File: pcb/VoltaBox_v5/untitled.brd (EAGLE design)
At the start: 100 x 80 mm, 46 parts, among them J1 1050170001, Q1 8 MHz, Q2 32768Hz, U1 MCU-STM32F103RCT6(LQFP64), U2 ADUM1401WTRWZ, U4 LMP92064SD/NOPB, X1 112J-TDAR-R(MICROSD)

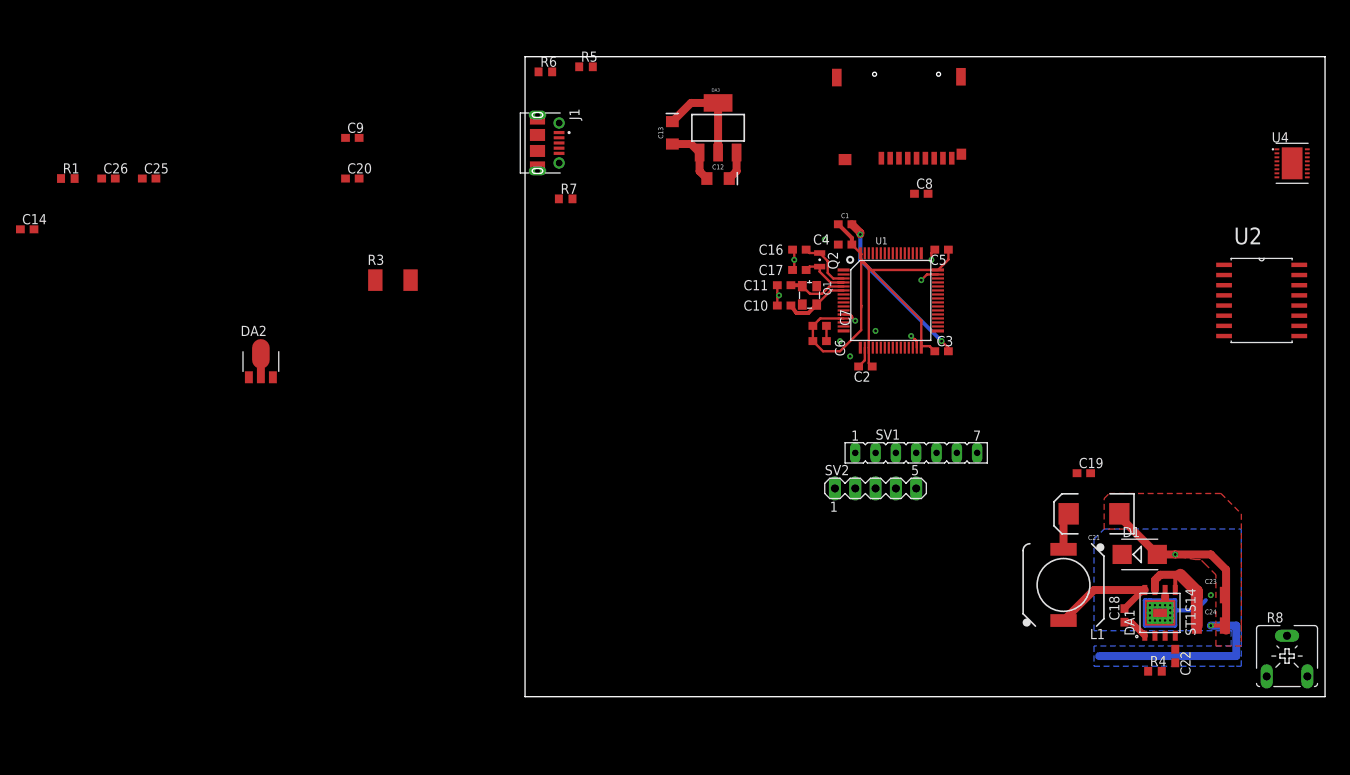
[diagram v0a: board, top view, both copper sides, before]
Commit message: Some PCB changes. ICs prefix changes. Added some capacitors. Q3 case type changed.
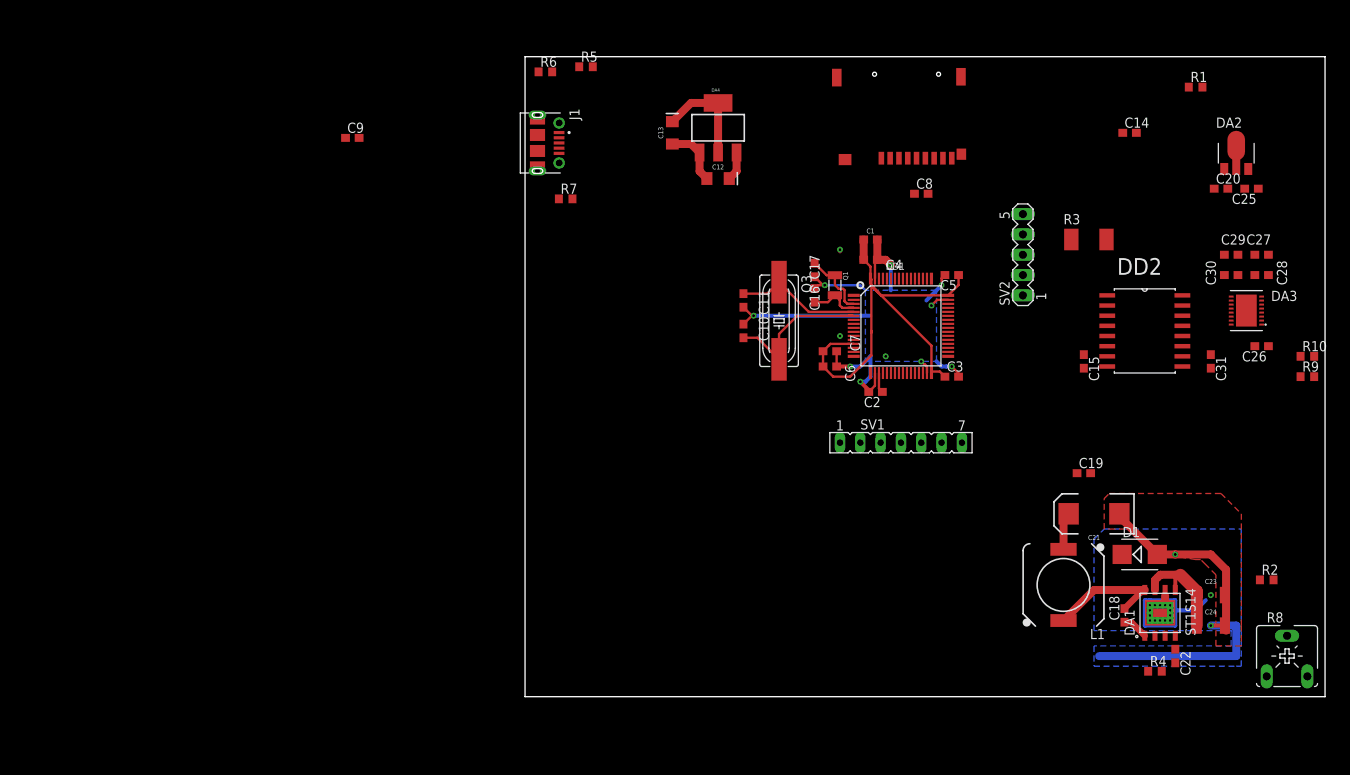
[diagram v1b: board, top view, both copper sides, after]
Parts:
- removed Q2: 32768Hz, crystal:FC-12M
- removed U1: MCU-STM32F103RCT6(LQFP64), MCU-STM32F103RCT6_LQFP64_:LQFP64-0.5-10X10MM
- removed U2: ADUM1401WTRWZ, ADUM1401WTRWZ:SOIC127P1032X265-16N
- removed U4: LMP92064SD/NOPB, LMP92064SD_NOPB:SON50P400X500X80-17N
- added C15, C28, C29, C31: 0.1u, eagle-ltspice:C0603
- added C27, C30: 10p, eagle-ltspice:C0603
- added DA4: (no value), SparkFun-IC-Power:SOT223
- added DD1: MCU-STM32F103RCT6(LQFP64), MCU-STM32F103RCT6_LQFP64_:LQFP64-0.5-10X10MM
- added DD2: ADUM1401WTRWZ, ADUM1401WTRWZ:SOIC127P1032X265-16N
- added Q3: 8MHz, crystal:HC49UP
- added R10, R2, R9: 3.3K, resistor:R0603
- DA3: value (none) -> LMP92064SD/NOPB; device SparkFun-IC-Power:SOT223 -> LMP92064SD_NOPB:SON50P400X500X80-17N
- Q1: value 8 MHz -> 32768Hz; device crystal-geyer_V1_0:3.2X2.5_KX-7 -> crystal-geyer_V1_0:3.2X1.5
- moved C26 145.7 mm to (92.1, 43.8), turned to 180 degrees
- moved R1 141.4 mm to (83.8, 76.2)
- moved C14 138.3 mm to (75.6, 70.5)
- moved C25 137.8 mm to (90.8, 63.5), turned to 180 degrees
- moved DA2 124.7 mm to (88.9, 67.9)
- moved C20 108.6 mm to (87.0, 63.5)
- moved R3 87.1 mm to (70.5, 57.1)
- moved DA3 69.9 mm to (90.2, 48.3), turned to 180 degrees
- moved SV2 34.5 mm to (62.2, 55.2), turned to 90 degrees
- moved C11 5.99 mm to (27.3, 45.7), turned to 90 degrees
- moved C10 5.43 mm to (27.3, 49.5), turned to 270 degrees
- moved C17 3.70 mm to (36.2, 50.2), turned to 90 degrees
- moved C1 3.70 mm to (43.2, 57.1)
- moved C4 3.70 mm to (43.2, 54.6), turned to 0 degrees
- moved C5 3.42 mm to (53.3, 52.7)
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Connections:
- new net N$24: R2.2, R8.A
- new net N$25: DA3.5, R10.1, R9.2
- net +3V3: now also C15.1, DA4.2, DA4.4, DD1.13, DD1.19, DD1.32, DD1.48, DD1.64, DD2.1, DD2.7; no longer DA3.2, DA3.4, U1.13, U1.19, U1.32, U1.48, U1.64, U2.1, U2.7
- net +4V: now also R10.2
- net +5V: now also C27.1, C28.1, C29.1, C30.1, C31.1, DA3.8, DA3.9, DD2.10, DD2.16; no longer U2.10, U2.16, U4.8, U4.9
- net ADC_MISO: now also DA3.11, DD1.35, DD2.6; no longer U1.35, U2.6, U4.11
- net ADC_MOSI: now also DD1.36, DD2.3; no longer U1.36, U2.3
- net ADC_NSS: now also DD1.33, DD2.5; no longer U1.33, U2.5
- net ADC_SCK: now also DD1.34, DD2.4; no longer U1.34, U2.4
- net GND: now also C15.2, C27.2, C28.2, C29.2, C30.2, C31.2, DA3.10, DA3.16, DA3.17, DA3.2, DA3.4, DA3.6, DA3.7, DA4.1, DD1.12, DD1.18, DD1.31, DD1.47, DD1.60, DD1.63, DD2.15, DD2.2, DD2.8, DD2.9, R2.1, R9.1; no longer DA3.1, R8.A, U1.12, U1.18, U1.31, U1.47, U1.60, U1.63, U2.15, U2.2, U2.8, U2.9, U4.10, U4.16, U4.2, U4.4, U4.6, U4.7
- net N$1: now also DD1.5, Q3.1; no longer Q1.1, U1.5
- net N$11: now also DA3.12, DD2.14; no longer U2.14, U4.12
- net N$13: now also DD1.54; no longer U1.54
- net N$14: now also DD1.53; no longer U1.53
- net N$15: now also DD1.52; no longer U1.52
- net N$16: now also DD1.51; no longer U1.51
- net N$18: now also DD1.40; no longer U1.40
- net N$19: now also DD1.39; no longer U1.39
- net N$2: now also DD1.6, Q3.2; no longer Q1.3, U1.6
- net N$20: now also DD1.45; no longer U1.45
- net N$21: now also DD1.44; no longer U1.44
- net N$23: now also DA3.3; no longer U4.3
- net N$3: now also DA3.1; no longer U4.1
- net N$5: now also DA3.13, DD2.13; no longer U2.13, U4.13
- net N$6: now also DA3.14, DD2.12; no longer U2.12, U4.14
- net N$7: now also DD1.4, Q1.2; no longer Q2.2, U1.4
- net N$8: now also DD1.3, Q1.1; no longer Q2.1, U1.3
- net NRESET: now also DD1.7; no longer U1.7
- net OLED_CS: now also DD1.50; no longer U1.50
- net OLED_DC: now also DD1.58; no longer U1.58
- net OLED_MOSI: now also DD1.57; no longer U1.57
- net OLED_RS: now also DD1.56; no longer U1.56
- net OLED_SCK: now also DD1.55; no longer U1.55
- net SWCLK: now also DD1.49; no longer U1.49
- net SWDIO: now also DD1.46; no longer U1.46
- net VCC: now also DA4.3; no longer DA3.3
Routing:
- net GND: track 116.6 -> 142.0 mm
- net N$2: track 8.22 -> 20.6 mm
- net +3V3: track 84.8 -> 75.4 mm
- net N$1: track 7.58 -> 15.9 mm
- net N$8: track 7.04 -> 8.52 mm

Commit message: DC-DC new layout, adc part implemented
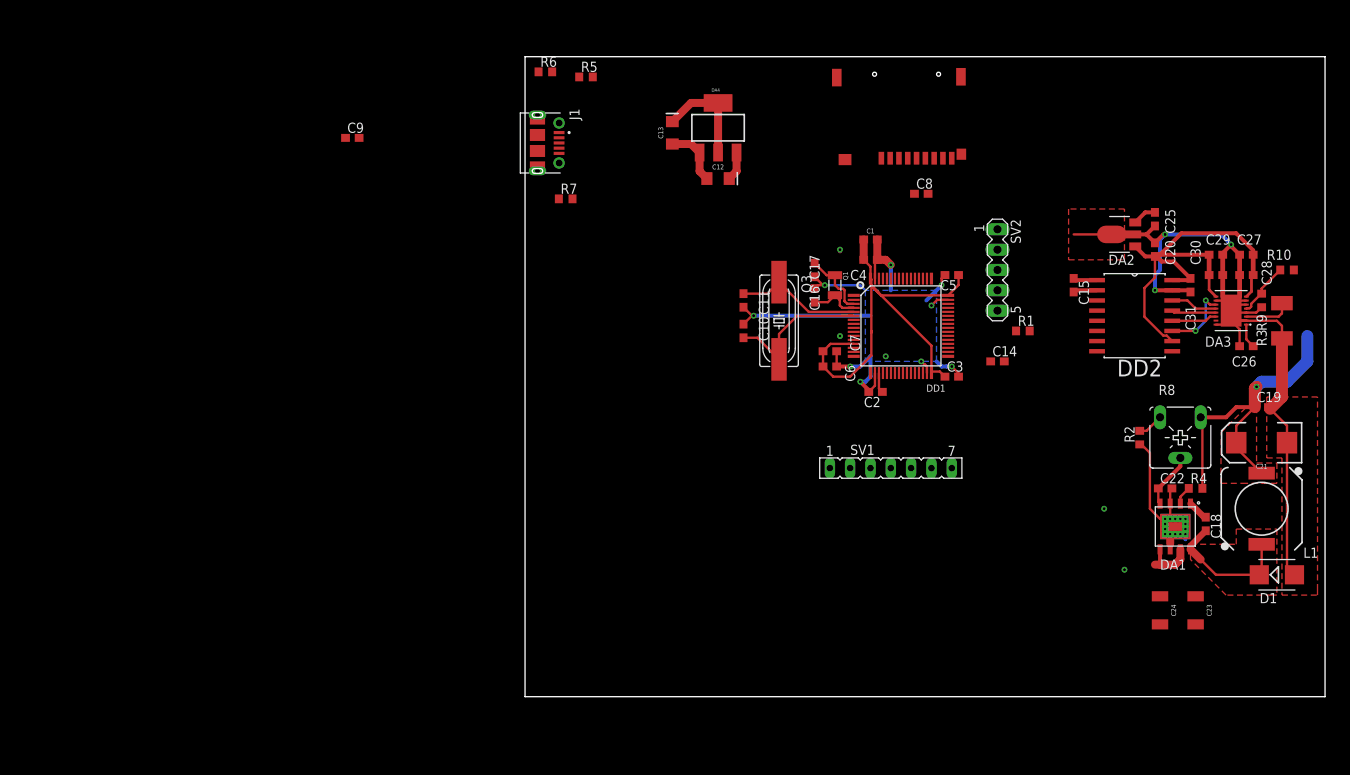
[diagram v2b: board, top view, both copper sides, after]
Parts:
- moved R1 37.4 mm to (62.2, 45.7)
- moved C14 33.0 mm to (59.1, 41.9)
- moved R8 30.4 mm to (81.9, 32.4), turned to 180 degrees
- moved L1 26.5 mm to (92.1, 23.5)
- moved R3 26.2 mm to (94.6, 47.0), turned to 90 degrees
- moved R2 23.8 mm to (76.8, 32.4), turned to 90 degrees
- moved C19 23.7 mm to (92.1, 36.2)
- moved R4 23.4 mm to (83.8, 26.0)
- moved C21 22.8 mm to (92.1, 31.8)
- moved C22 21.0 mm to (80.0, 26.0), turned to 0 degrees
- moved DA2 17.8 mm to (74.3, 57.8), turned to 90 degrees
- moved DA1 17.5 mm to (83.2, 24.1), turned to 270 degrees
- moved D1 17.3 mm to (94.0, 15.2)
- moved C18 15.3 mm to (85.1, 21.6), turned to 270 degrees
- moved C25 12.7 mm to (78.7, 59.7), turned to 270 degrees
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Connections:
- removed net N$24: R2.2, R8.A
- new net N$22: R2.2, R8.E
- new net N$26: DA3.11, DD2.11
- net +4V: now also R8.A; no longer R8.E
- net ADC_MISO: no longer DA3.11
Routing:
- net +5V: track 0.00 -> 56.3 mm
- net GND: track 142.0 -> 192.6 mm, vias 14 -> 17
- net +4V: track 4.71 -> 40.1 mm, vias 0 -> 1
- net N$26: track 0.00 -> 8.75 mm, vias 0 -> 2
- net N$10: track 0.00 -> 6.95 mm
- net N$25: track 0.00 -> 6.81 mm
- net N$23: track 0.00 -> 6.31 mm
- net N$11: track 0.00 -> 5.89 mm
- net N$6: track 0.00 -> 5.68 mm
- net N$5: track 0.00 -> 5.57 mm
- net +12V: track 13.8 -> 9.58 mm
- net N$9: track 15.2 -> 18.7 mm
- net N$22: track 0.00 -> 3.24 mm, vias 1 -> 0
- net N$3: track 0.00 -> 3.05 mm
- net +3V3: track 75.4 -> 78.4 mm
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- added copper zone on layer 1, net +4V
- added copper zone on layer 1, net N$9

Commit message: micro usb to usb-b, dc-dc inductor replaced, some schematic changes
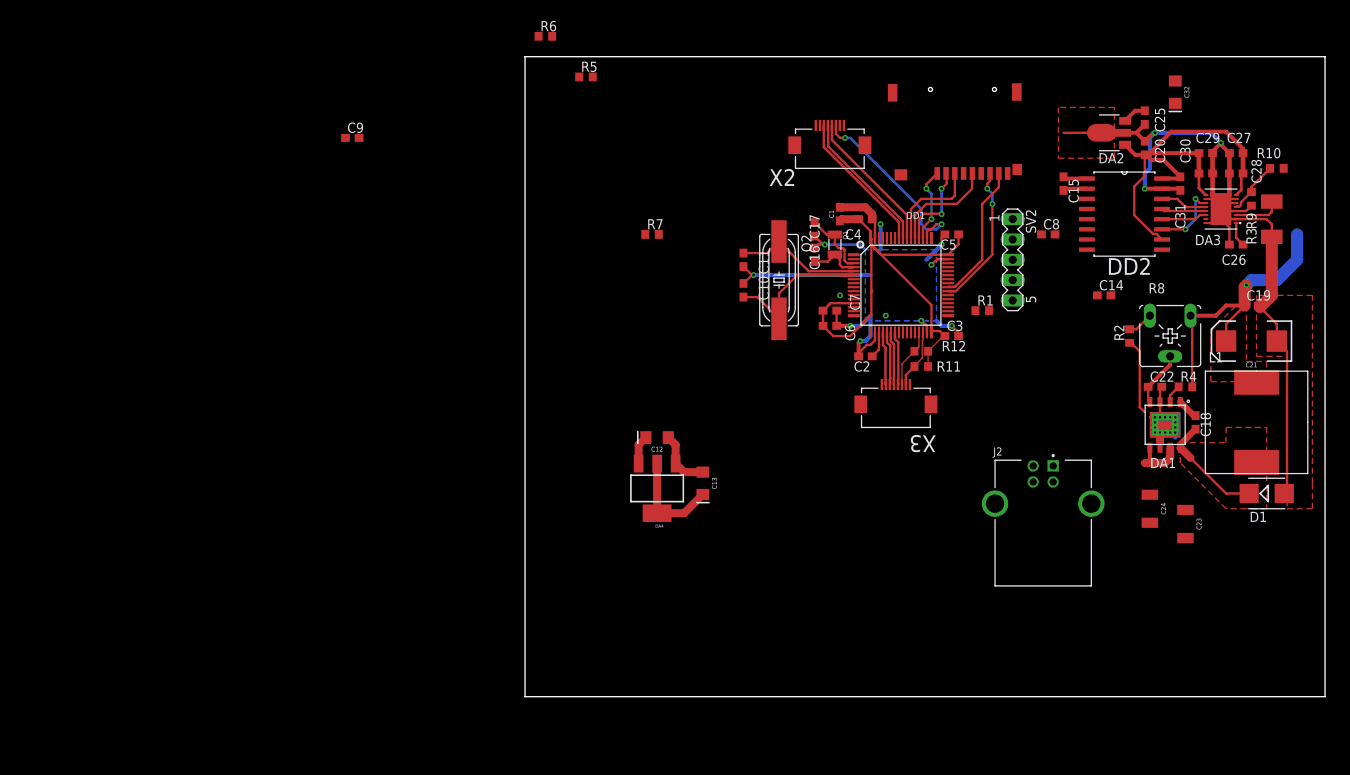
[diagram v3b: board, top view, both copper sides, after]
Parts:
- removed J1: 1050170001, 1050170001:MOLEX_1050170001
- removed Q3: 8MHz, crystal:HC49UP
- removed SV1: (no value), con-lsta:FE07
- added C32: 10uF, SparkFun-Capacitors:EIA3216
- added J2: 292304-3, 292304-3:TE_292304-3
- added Q2: 8MHz, crystal:HC49UP
- added R11, R12: 10k, resistor:R0603
- added X2, X3: 52892-0895, 52892-0895:MOLEX_52892-0895
- L1: value 8.5u -> B82477G4; device untitled:DR1030 -> untitled:B82477G4
- moved DA4 45.7 mm to (16.5, 26.0), turned to 180 degrees
- moved C13 44.0 mm to (22.2, 26.7), turned to 270 degrees
- moved C12 33.3 mm to (16.5, 32.4), turned to 180 degrees
- moved C8 16.7 mm to (65.4, 57.8)
- moved C14 15.7 mm to (72.4, 50.2)
- moved R8 12.8 mm to (80.6, 45.1)
- moved C15 12.8 mm to (67.3, 64.1)
- moved C18 12.8 mm to (83.8, 34.3)
- moved C19 12.8 mm to (90.8, 48.9)
- moved C21 12.8 mm to (90.8, 44.5)
- moved C22 12.8 mm to (78.7, 38.7)
- moved C25 12.8 mm to (77.5, 72.4)
- moved C26 12.8 mm to (88.9, 56.5)
- moved C28 12.8 mm to (88.9, 65.4)
- moved C30 12.8 mm to (85.1, 65.4)
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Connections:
- new net GND1: X2.8
- new net N$24: DD1.30, R11.1, X3.7
- new net N$27: DD1.29, R12.1, X3.6
- new net N$28: DD1.23, X3.5
- new net N$29: DD1.22, X3.4
- new net N$30: DD1.21, X3.3
- new net N$31: DD1.20, X3.2
- net +3V3: now also R11.2, R12.2, X2.1, X3.1; no longer SV1.2
- net +4V: now also L1.P$2; no longer L1.2
- net +5V: now also C32.+
- net DM: now also J2.2; no longer J1.2
- net DP: now also J2.3; no longer J1.3
- net GND: now also C32.-, J2.4, J2.SH1, J2.SH2, X3.8; no longer J1.5, J1.SH1, J1.SH2, J1.SH3, J1.SH4, J1.SH5, J1.SH6, J1.SH7, J1.SH8, SV1.1
- net N$1: now also Q2.1; no longer Q3.1
- net N$2: now also Q2.2; no longer Q3.2
- net N$9: now also L1.P$1; no longer L1.1
- net OLED_CS: now also X2.6; no longer SV1.7
- net OLED_DC: now also X2.2; no longer SV1.6
- net OLED_MOSI: now also X2.3; no longer SV1.4
- net OLED_RS: now also X2.4; no longer SV1.5
- net OLED_SCK: now also X2.5; no longer SV1.3
- net VCC: now also J2.1; no longer J1.1
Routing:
- net OLED_CS: track 0.00 -> 23.6 mm, vias 0 -> 2
- net N$19: track 0.00 -> 18.0 mm, vias 0 -> 2
- net OLED_MOSI: track 0.00 -> 18.0 mm
- net OLED_RS: track 0.00 -> 18.0 mm
- net OLED_SCK: track 0.00 -> 18.0 mm
- net N$18: track 0.00 -> 17.3 mm
- net N$14: track 0.00 -> 13.3 mm
- net N$13: track 0.00 -> 12.6 mm
- net N$15: track 0.00 -> 10.9 mm, vias 0 -> 2
- net N$16: track 0.00 -> 9.34 mm, vias 0 -> 2
- net N$24: track 0.00 -> 7.41 mm
- net N$27: track 0.00 -> 7.40 mm
- net N$28: track 0.00 -> 6.72 mm
- net N$30: track 0.00 -> 6.71 mm
- net N$29: track 0.00 -> 6.69 mm
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
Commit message: Some pcb changes, dc-dc capacitors replaced.
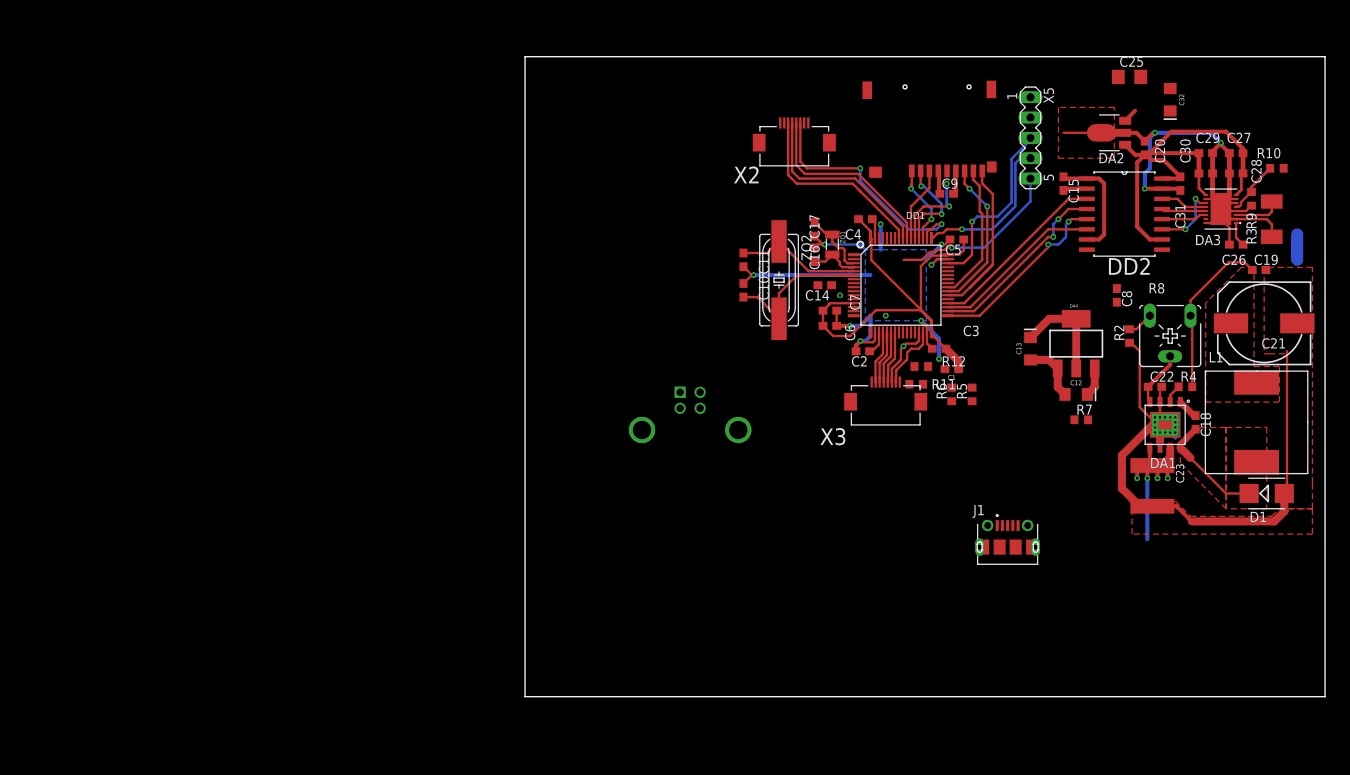
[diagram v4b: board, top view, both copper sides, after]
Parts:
- removed C24: 10uF, SparkFun-Capacitors:1210
- removed J2: 292304-3, 292304-3:TE_292304-3
- removed Q1: 32768Hz, crystal-geyer_V1_0:3.2X1.5
- removed R1: 10K, resistor:R0603
- removed SV2: (no value), con-lstb:MA05-1
- added J1: 1050170001, 1050170001:MOLEX_1050170001
- added X4: 292304-3, 292304-3:TE_292304-3
- added X5: (no value), con-lstb:MA05-1
- added ZQ1: 32768Hz, crystal-geyer_V1_0:3.2X1.5
- C21: value 100uF -> 100u; device SparkFun-Capacitors:EIA7343 -> rcl:150CLZ-1014
- C23: value 10uF -> 4.7u; device SparkFun-Capacitors:1210 -> rcl:C2220K
- C25: device eagle-ltspice:C0603 -> eagle-ltspice:C1206
- C9: value 10n -> 1u
- R10: value 3.3K -> 2.7K
- R9: value 3.3K -> 1.2K
- moved C9 74.6 mm to (52.7, 62.9)
- moved R6 67.7 mm to (53.3, 37.8), turned to 90 degrees
- moved R5 62.5 mm to (55.9, 37.8), turned to 90 degrees
- moved R7 58.4 mm to (69.5, 34.6)
- moved DA4 55.4 mm to (68.9, 44.1), turned to 0 degrees
- moved C12 52.7 mm to (68.9, 37.8), turned to 0 degrees
- moved C13 44.3 mm to (63.2, 43.5), turned to 90 degrees
- moved C14 34.9 mm to (37.5, 51.4), turned to 180 degrees
- moved C1 23.9 mm to (53.3, 41.0), turned to 180 degrees
- moved C8 11.5 mm to (74.0, 50.2), turned to 270 degrees
- moved C23 6.30 mm to (78.4, 26.4)
- moved C25 5.43 mm to (75.6, 77.5), turned to 0 degrees
- moved C19 4.55 mm to (91.8, 53.3)
- moved X2 4.46 mm to (33.7, 74.6)
- moved X1 3.19 mm to (57.1, 65.7)
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- renumbered Q2 to ZQ2
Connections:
- removed net GND1: X2.8
- removed net N$17: X1.P$9
- new net N$32: DD1.38, X1.P$9
- net +12V: no longer C24.1
- net +3V3: now also C9.1, R7.2, X5.1; no longer R1.2, SV2.1
- net +4V: now also C21.+; no longer C21.A
- net DM: now also X4.2; no longer J2.2
- net DP: now also X4.3; no longer J2.3
- net GND: now also C21.-, C9.2, X2.8, X4.4, X4.SH1, X4.SH2, X5.2; no longer C21.C, C24.2, J2.4, J2.SH1, J2.SH2, SV2.2
- net N$7: now also ZQ1.2; no longer Q1.2
- net N$8: now also ZQ1.1; no longer Q1.1
- net NRESET: now also X5.5; no longer R1.1, SV2.5
- net SWCLK: now also X5.4; no longer SV2.4
- net SWDIO: now also X5.3; no longer SV2.3
- net VCC: now also X4.1; no longer J2.1, R7.2
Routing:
- net ADC_SCK: track 0.00 -> 23.6 mm, vias 0 -> 2
- net N$32: track 0.00 -> 23.5 mm
- net ADC_NSS: track 0.00 -> 23.5 mm, vias 0 -> 2
- net ADC_MOSI: track 0.00 -> 22.7 mm
- net SWDIO: track 0.00 -> 22.5 mm, vias 0 -> 1
- net NRESET: track 0.00 -> 21.8 mm, vias 0 -> 1
- net ADC_MISO: track 0.00 -> 21.4 mm
- net SWCLK: track 0.00 -> 19.7 mm, vias 0 -> 1
- net GND: track 196.6 -> 213.5 mm
- net +12V: track 9.58 -> 23.4 mm, vias 0 -> 4
- net +3V3: track 84.2 -> 96.7 mm
- net +4V: track 35.7 -> 24.1 mm, vias 1 -> 0
- net OLED_CS: track 23.6 -> 30.2 mm
- net OLED_MOSI: track 18.0 -> 24.4 mm
- net OLED_RS: track 18.0 -> 24.2 mm
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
